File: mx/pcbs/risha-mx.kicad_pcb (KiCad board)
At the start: 2 copper layers, 100 x 95.3 mm, 19 parts

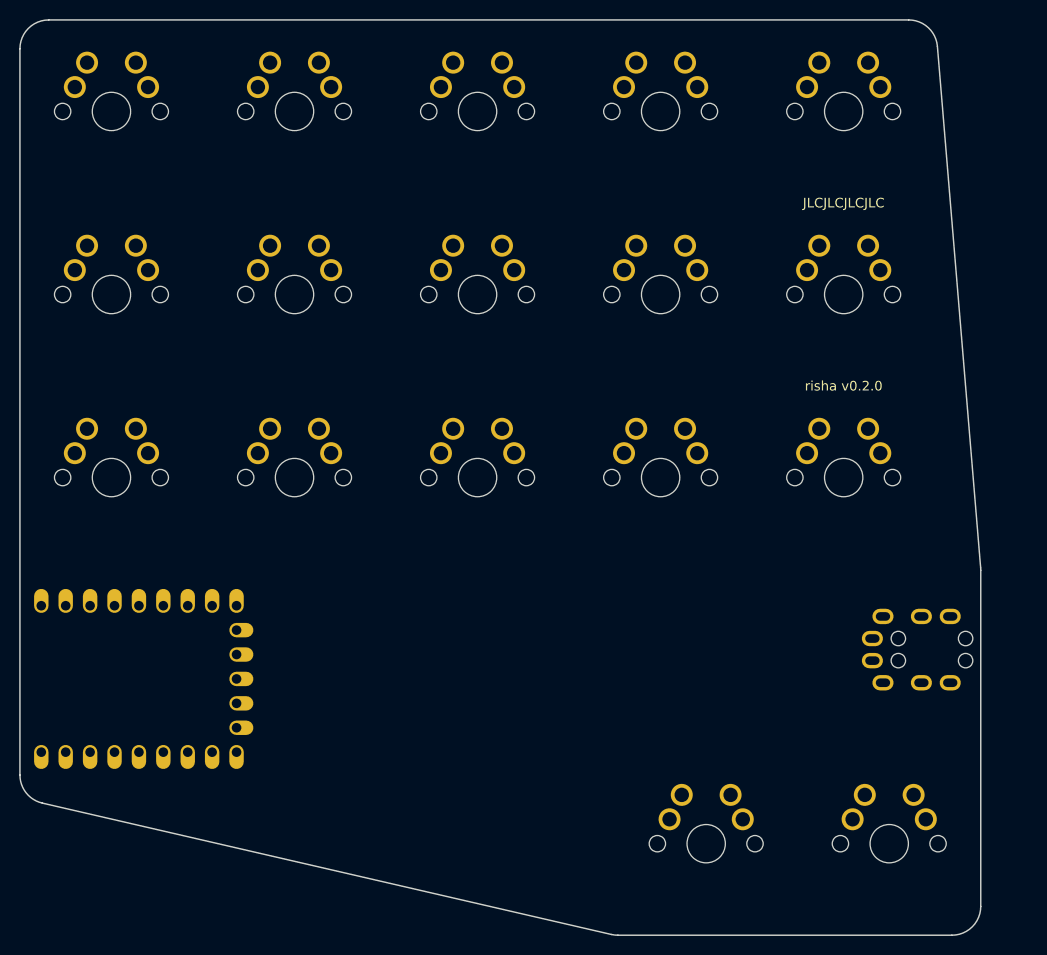
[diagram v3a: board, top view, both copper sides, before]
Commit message: outline tweaks for ergonomics
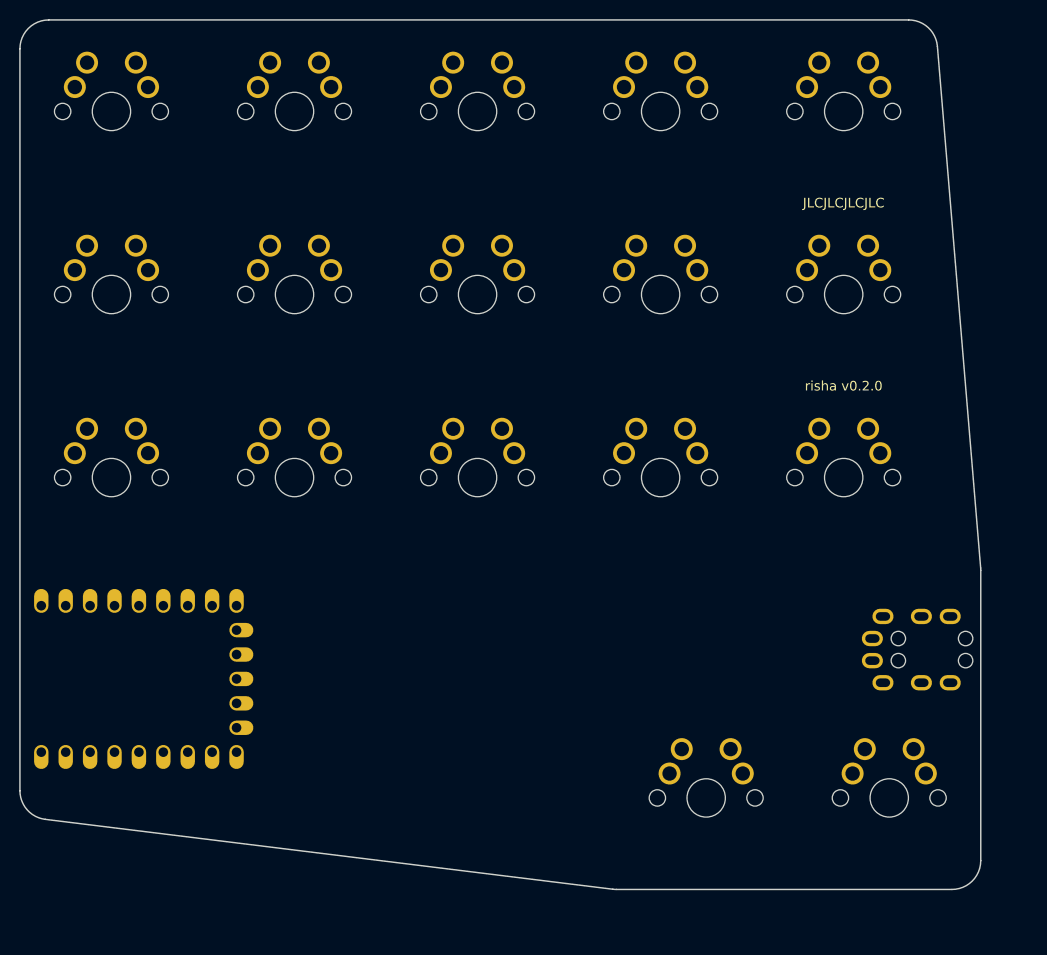
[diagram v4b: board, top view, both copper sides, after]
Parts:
- moved S16 4.76 mm to (214.3, 185.7)
- moved S17 4.76 mm to (233.3, 185.7)
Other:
- board size 100 x 95.3 mm -> 100 x 90.5 mm
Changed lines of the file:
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@@
           )
       (module MX (layer F.Cu)
-      (at 214.29000000000002 190.5 0)
+      (at 214.29000000000002 185.7375 0)
       (fp_text reference "S16" (at 0 0) (layer F.SilkS) hide (effects (font (size 1.27 1.27) (thickness 0.15))))
       (fp_text value "" (at 0 0) (layer F.SilkS) hide (effects (font (size 1.27 1.27) (thickness 0.15))))
@@
           )
       (module MX (layer F.Cu)
-      (at 233.34000000000003 190.5 0)
+      (at 233.34000000000003 185.7375 0)
       (fp_text reference "S17" (at 0 0) (layer F.SilkS) hide (effects (font (size 1.27 1.27) (thickness 0.15))))
       (fp_text value "" (at 0 0) (layer F.SilkS) hide (effects (font (size 1.27 1.27) (thickness 0.15))))
@@
                 (effects (font (size 1 1) (thickness 0.15)) )
             )
-            (gr_line (start 142.875 183.35115725804656) (end 142.875 107.77499999999999) (angle 90) (layer Edge.Cuts) (width 0.15))
+            (gr_line (start 142.875 184.98921209311683) (end 142.875 107.77499999999999) (angle 90) (layer Edge.Cuts) (width 0.15))
 (gr_line (start 145.875 104.77499999999999) (end 235.3635180643045 104.77499999999999) (angle 90) (layer Edge.Cuts) (width 0.15))
-(gr_line (start 238.35325257322498 107.52703260755379) (end 242.85473450892053 161.80122936388307) (angle 90) (layer Edge.Cuts) (width 0.15))
-(gr_line (start 242.86500000000004 162.0491967563289) (end 242.86500000000004 197.025) (angle 90) (layer Edge.Cuts) (width 0.15))
-(gr_line (start 239.86500000000004 200.025) (end 205.10678493784775 200.025) (angle 90) (layer Edge.Cuts) (width 0.15))
-(gr_line (start 204.43197365470533 199.94811982697692) (end 145.20018871685755 186.2742770850235) (angle 90) (layer Edge.Cuts) (width 0.15))
+(gr_line (start 238.35325257322495 107.52703260755379) (end 242.85473450892053 161.80122936388352) (angle 90) (layer Edge.Cuts) (width 0.15))
+(gr_line (start 242.865 162.04919675632937) (end 242.865 192.26250000000002) (angle 90) (layer Edge.Cuts) (width 0.15))
+(gr_line (start 239.865 195.26250000000002) (end 204.94898799960643 195.26250000000002) (angle 90) (layer Edge.Cuts) (width 0.15))
+(gr_line (start 204.58239128598487 195.2400169106351) (end 145.5084032863784 187.96672900375188) (angle 90) (layer Edge.Cuts) (width 0.15))
 (gr_arc (start 145.875 107.77499999999999) (end 145.875 104.77499999999999) (angle -90) (layer Edge.Cuts) (width 0.15))
-(gr_arc (start 235.3635180643045 107.77499999999999) (end 238.35325256430448 107.5270326) (angle -85.25876255983368) (layer Edge.Cuts) (width 0.15))
-(gr_arc (start 239.86500000000004 162.0491967563289) (end 242.86500000000004 162.0491967563289) (angle -4.741237440159549) (layer Edge.Cuts) (width 0.15))
-(gr_arc (start 239.86500000000004 197.025) (end 239.86500000000004 200.025) (angle -90) (layer Edge.Cuts) (width 0.15))
-(gr_arc (start 205.10678493784775 197.025) (end 204.43197363784776 199.9481199) (angle -12.999179268914816) (layer Edge.Cuts) (width 0.15))
-(gr_arc (start 145.875 183.35115725804656) (end 142.875 183.35115725804656) (angle -77.00082073108479) (layer Edge.Cuts) (width 0.15))
+(gr_arc (start 235.3635180643045 107.77499999999999) (end 238.35325256430448 107.5270326) (angle -85.25876255983363) (layer Edge.Cuts) (width 0.15))
+(gr_arc (start 239.865 162.04919675632937) (end 242.865 162.04919675632937) (angle -4.741237440159497) (layer Edge.Cuts) (width 0.15))
+(gr_arc (start 239.865 192.26250000000002) (end 239.865 195.26250000000002) (angle -90) (layer Edge.Cuts) (width 0.15))
+(gr_arc (start 204.94898799960643 192.26250000000002) (end 204.58239129960643 195.24001690000003) (angle -7.019024613723559) (layer Edge.Cuts) (width 0.15))
+(gr_arc (start 145.875 184.98921209311683) (end 142.875 184.98921209311683) (angle -82.98097538627582) (layer Edge.Cuts) (width 0.15))
 )

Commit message: hacky sub 100mm^2 idea for rear-facing trrs
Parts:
- added S18: , MX, F.Cu at (237.4, 176.2)
- added _4: , MountingHole_2.2mm_M2_Pad_Via, F.Cu at (208.8, 166.7)
- added _5: , MountingHole_2.2mm_M2_Pad_Via, F.Cu at (161.9, 123.8)
- added _6: , MountingHole_2.2mm_M2_Pad_Via, F.Cu at (219.1, 123.8)
- moved TRRS1 19.1 mm to (243.8, 152.4), turned to 0 degrees
- moved S16 17.8 mm to (199.3, 176.2)
- moved S17 17.8 mm to (218.3, 176.2)
- moved ? 2.22 mm to (156.4, 171.5)
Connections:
- ? pad 10: GP9 -> matrix_index_top
- ? pad 11: matrix_middle_bottom -> matrix_index_home
- ? pad 12: matrix_index_top -> matrix_index_bottom
- ? pad 13: matrix_index_home -> GP12
- ? pad 14: matrix_index_bottom -> matrix_inner_bottom
- ? pad 15: matrix_inner_bottom -> matrix_inner_home
- ? pad 16: matrix_inner_home -> matrix_inner_top
- ? pad 17: matrix_inner_top -> thumbfan_near_home
- ? pad 18: thumbfan_near_home -> thumbfan_middle_home
- ? pad 9: GP8 -> matrix_middle_bottom
- S17 pad 1: thumbfan_far_home -> thumbfan_middle_home
- TRRS1 pad 1: 3V3 -> GND
- TRRS1 pad 3: GP9 -> 3V3
- TRRS1 pad 4: GP8 -> GP12
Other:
- board size 100 x 90.5 mm -> 100 x 81 mm

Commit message: risha v0.2.0
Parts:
- turned S1 to 180 degrees
- turned S10 to 180 degrees
- turned S11 to 180 degrees
- turned S12 to 180 degrees
- turned S13 to 180 degrees
- turned S14 to 180 degrees
- turned S15 to 180 degrees
- turned S16 to 180 degrees
- turned S17 to 180 degrees
- turned S18 to 180 degrees
- turned S2 to 180 degrees
- turned S3 to 180 degrees
- turned S4 to 180 degrees
- turned S5 to 180 degrees
- turned S6 to 180 degrees
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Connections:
- ? pad 1: matrix_pinky_top -> matrix_pinky_bottom
- ? pad 14: matrix_inner_bottom -> matrix_inner_top
- ? pad 16: matrix_inner_top -> matrix_inner_bottom
- ? pad 3: matrix_pinky_bottom -> matrix_pinky_top
- ? pad 4: matrix_ring_bottom -> matrix_ring_top
- ? pad 6: matrix_ring_top -> matrix_ring_bottom
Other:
- outline, holes or cut-outs redrawn
